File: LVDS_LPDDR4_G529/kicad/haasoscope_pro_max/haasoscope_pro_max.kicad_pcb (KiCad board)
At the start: 10 copper layers, 200 x 125 mm, 8 parts, among them IC1 ADC12DL500ACF_Aligned, U1 MT53D512M16D1DS_Aligned, U2 FT601Q_Aligned, U3 Ti90G529_Functions

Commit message: add labels for all lvds_rx nets
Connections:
- net Net-(IC1A-DA1+) renamed /fpga_adc/lvds_rx3_2_P
- net Net-(IC1A-DA1-) renamed /fpga_adc/lvds_rx3_2_N
- net Net-(IC1A-DA10+) renamed /fpga_adc/lvds_rx3_11_P
- net Net-(IC1A-DA10-) renamed /fpga_adc/lvds_rx3_11_N
- net Net-(IC1A-DA11+) renamed /fpga_adc/lvds_rx3_12_P
- net Net-(IC1A-DA11-) renamed /fpga_adc/lvds_rx3_12_N
- net Net-(IC1A-DA2+) renamed /fpga_adc/lvds_rx3_3_P
- net Net-(IC1A-DA2-) renamed /fpga_adc/lvds_rx3_3_N
- net Net-(IC1A-DA3+) renamed /fpga_adc/lvds_rx3_4_P
- net Net-(IC1A-DA3-) renamed /fpga_adc/lvds_rx3_4_N
- net Net-(IC1A-DA4+) renamed /fpga_adc/lvds_rx3_5_P
- net Net-(IC1A-DA4-) renamed /fpga_adc/lvds_rx3_5_N
- net Net-(IC1A-DA5+) renamed /fpga_adc/lvds_rx3_6_P
- net Net-(IC1A-DA5-) renamed /fpga_adc/lvds_rx3_6_N
- net Net-(IC1A-DA6+) renamed /fpga_adc/lvds_rx3_7_P
- net Net-(IC1A-DA6-) renamed /fpga_adc/lvds_rx3_7_N
- net Net-(IC1A-DA7+) renamed /fpga_adc/lvds_rx3_8_P
- net Net-(IC1A-DA7-) renamed /fpga_adc/lvds_rx3_8_N
- net Net-(IC1A-DA8+) renamed /fpga_adc/lvds_rx3_9_P
- net Net-(IC1A-DA8-) renamed /fpga_adc/lvds_rx3_9_N
- net Net-(IC1A-DA9+) renamed /fpga_adc/lvds_rx3_10_P
- net Net-(IC1A-DA9-) renamed /fpga_adc/lvds_rx3_10_N
- net Net-(IC1A-DASTR+) renamed /fpga_adc/lvds_rx3_13_P
- net Net-(IC1A-DASTR-) renamed /fpga_adc/lvds_rx3_13_N
- net Net-(IC1A-DC0+) renamed /fpga_adc/lvds_rx4_1_P
- net Net-(IC1A-DC0-) renamed /fpga_adc/lvds_rx4_1_N
- net Net-(IC1A-DC1+) renamed /fpga_adc/lvds_rx4_2_P
- net Net-(IC1A-DC1-) renamed /fpga_adc/lvds_rx4_2_N
- net Net-(IC1A-DC10+) renamed /fpga_adc/lvds_rx4_11_P
- net Net-(IC1A-DC10-) renamed /fpga_adc/lvds_rx4_11_N
- net Net-(IC1A-DC11+) renamed /fpga_adc/lvds_rx4_12_P
- net Net-(IC1A-DC11-) renamed /fpga_adc/lvds_rx4_12_N
- net Net-(IC1A-DC2+) renamed /fpga_adc/lvds_rx4_3_P
- net Net-(IC1A-DC2-) renamed /fpga_adc/lvds_rx4_3_N
- net Net-(IC1A-DC3+) renamed /fpga_adc/lvds_rx4_4_P
- net Net-(IC1A-DC3-) renamed /fpga_adc/lvds_rx4_4_N
- net Net-(IC1A-DC4+) renamed /fpga_adc/lvds_rx4_5_P
- net Net-(IC1A-DC4-) renamed /fpga_adc/lvds_rx4_5_N
- net Net-(IC1A-DC5+) renamed /fpga_adc/lvds_rx4_6_P
- net Net-(IC1A-DC5-) renamed /fpga_adc/lvds_rx4_6_N
- net Net-(IC1A-DC6+) renamed /fpga_adc/lvds_rx4_7_P
- net Net-(IC1A-DC6-) renamed /fpga_adc/lvds_rx4_7_N
- net Net-(IC1A-DC7+) renamed /fpga_adc/lvds_rx4_8_P
- net Net-(IC1A-DC7-) renamed /fpga_adc/lvds_rx4_8_N
- net Net-(IC1A-DC8+) renamed /fpga_adc/lvds_rx4_9_P
- net Net-(IC1A-DC8-) renamed /fpga_adc/lvds_rx4_9_N
- net Net-(IC1A-DC9+) renamed /fpga_adc/lvds_rx4_10_P
- net Net-(IC1A-DC9-) renamed /fpga_adc/lvds_rx4_10_N
- net Net-(IC1A-DCSTR+) renamed /fpga_adc/lvds_rx4_13_P
- net Net-(IC1A-DCSTR-) renamed /fpga_adc/lvds_rx4_13_N
- net Net-(IC1B-DB1+) renamed /fpga_adc/lvds_rx1_2_P
- net Net-(IC1B-DB1-) renamed /fpga_adc/lvds_rx1_2_N
- net Net-(IC1B-DB10+) renamed /fpga_adc/lvds_rx1_11_P
- net Net-(IC1B-DB10-) renamed /fpga_adc/lvds_rx1_11_N
- net Net-(IC1B-DB11+) renamed /fpga_adc/lvds_rx1_12_P
- net Net-(IC1B-DB11-) renamed /fpga_adc/lvds_rx1_12_N
- net Net-(IC1B-DB2+) renamed /fpga_adc/lvds_rx1_3_P
- net Net-(IC1B-DB2-) renamed /fpga_adc/lvds_rx1_3_N
- net Net-(IC1B-DB3+) renamed /fpga_adc/lvds_rx1_4_P
- net Net-(IC1B-DB3-) renamed /fpga_adc/lvds_rx1_4_N
- net Net-(IC1B-DB4+) renamed /fpga_adc/lvds_rx1_5_P
- net Net-(IC1B-DB4-) renamed /fpga_adc/lvds_rx1_5_N
- net Net-(IC1B-DB5+) renamed /fpga_adc/lvds_rx1_6_P
- net Net-(IC1B-DB5-) renamed /fpga_adc/lvds_rx1_6_N
- net Net-(IC1B-DB6+) renamed /fpga_adc/lvds_rx1_7_P
- net Net-(IC1B-DB6-) renamed /fpga_adc/lvds_rx1_7_N
- net Net-(IC1B-DB7+) renamed /fpga_adc/lvds_rx1_8_P
- net Net-(IC1B-DB7-) renamed /fpga_adc/lvds_rx1_8_N
- net Net-(IC1B-DB8+) renamed /fpga_adc/lvds_rx1_9_P
- net Net-(IC1B-DB8-) renamed /fpga_adc/lvds_rx1_9_N
- net Net-(IC1B-DB9+) renamed /fpga_adc/lvds_rx1_10_P
- net Net-(IC1B-DB9-) renamed /fpga_adc/lvds_rx1_10_N
- net Net-(IC1B-DBSTR+) renamed /fpga_adc/lvds_rx1_13_P
- net Net-(IC1B-DBSTR-) renamed /fpga_adc/lvds_rx1_13_N
- net Net-(IC1B-DD0+) renamed /fpga_adc/lvds_rx2_1_P
- net Net-(IC1B-DD0-) renamed /fpga_adc/lvds_rx2_1_N
- net Net-(IC1B-DD1+) renamed /fpga_adc/lvds_rx2_2_P
- net Net-(IC1B-DD1-) renamed /fpga_adc/lvds_rx2_2_N
- net Net-(IC1B-DD10+) renamed /fpga_adc/lvds_rx2_11_P
- net Net-(IC1B-DD10-) renamed /fpga_adc/lvds_rx2_11_N
- net Net-(IC1B-DD11+) renamed /fpga_adc/lvds_rx2_12_P
- net Net-(IC1B-DD11-) renamed /fpga_adc/lvds_rx2_12_N
- net Net-(IC1B-DD2+) renamed /fpga_adc/lvds_rx2_3_P
- net Net-(IC1B-DD2-) renamed /fpga_adc/lvds_rx2_3_N
- net Net-(IC1B-DD3+) renamed /fpga_adc/lvds_rx2_4_P
- net Net-(IC1B-DD3-) renamed /fpga_adc/lvds_rx2_4_N
- net Net-(IC1B-DD4+) renamed /fpga_adc/lvds_rx2_5_P
- net Net-(IC1B-DD4-) renamed /fpga_adc/lvds_rx2_5_N
- net Net-(IC1B-DD5+) renamed /fpga_adc/lvds_rx2_6_P
- net Net-(IC1B-DD5-) renamed /fpga_adc/lvds_rx2_6_N
- net Net-(IC1B-DD6+) renamed /fpga_adc/lvds_rx2_7_P
- net Net-(IC1B-DD6-) renamed /fpga_adc/lvds_rx2_7_N
- net Net-(IC1B-DD7+) renamed /fpga_adc/lvds_rx2_8_P
- net Net-(IC1B-DD7-) renamed /fpga_adc/lvds_rx2_8_N
- net Net-(IC1B-DD8+) renamed /fpga_adc/lvds_rx2_9_P
- net Net-(IC1B-DD8-) renamed /fpga_adc/lvds_rx2_9_N
- net Net-(IC1B-DD9+) renamed /fpga_adc/lvds_rx2_10_P
- net Net-(IC1B-DD9-) renamed /fpga_adc/lvds_rx2_10_N
- net Net-(IC1B-DDSTR+) renamed /fpga_adc/lvds_rx2_13_P
- net Net-(IC1B-DDSTR-) renamed /fpga_adc/lvds_rx2_13_N
- net Net-(IC1C-DACLK+) renamed /fpga_adc/lvds_rx_top_clkin3_P
- net Net-(IC1C-DACLK-) renamed /fpga_adc/lvds_rx_top_clkin3_N
- net Net-(IC1C-DBCLK+) renamed /fpga_adc/lvds_rx_top_clkin1_P
- net Net-(IC1C-DBCLK-) renamed /fpga_adc/lvds_rx_top_clkin1_N
- net Net-(IC1C-DCCLK+) renamed /fpga_adc/lvds_rx_top_clkin4_P
- net Net-(IC1C-DCCLK-) renamed /fpga_adc/lvds_rx_top_clkin4_N
- net Net-(IC1C-DDCLK+) renamed /fpga_adc/lvds_rx_top_clkin2_P
- net Net-(IC1C-DDCLK-) renamed /fpga_adc/lvds_rx_top_clkin2_N

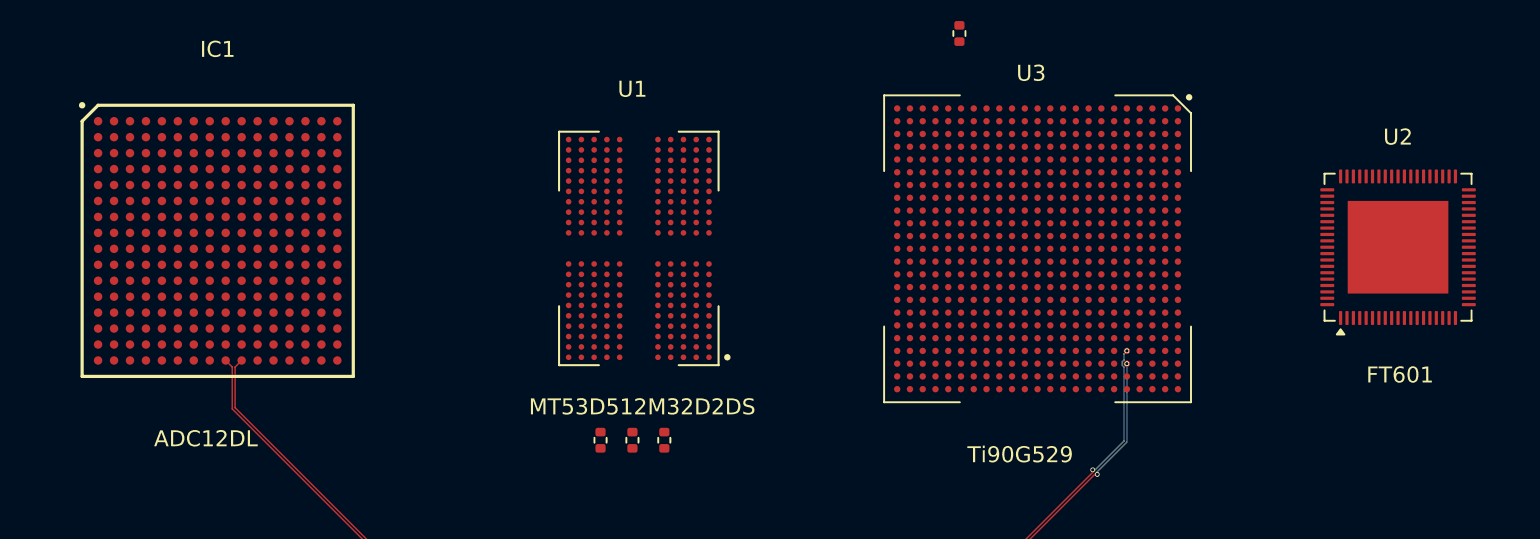
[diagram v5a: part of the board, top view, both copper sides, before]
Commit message: vias in pad
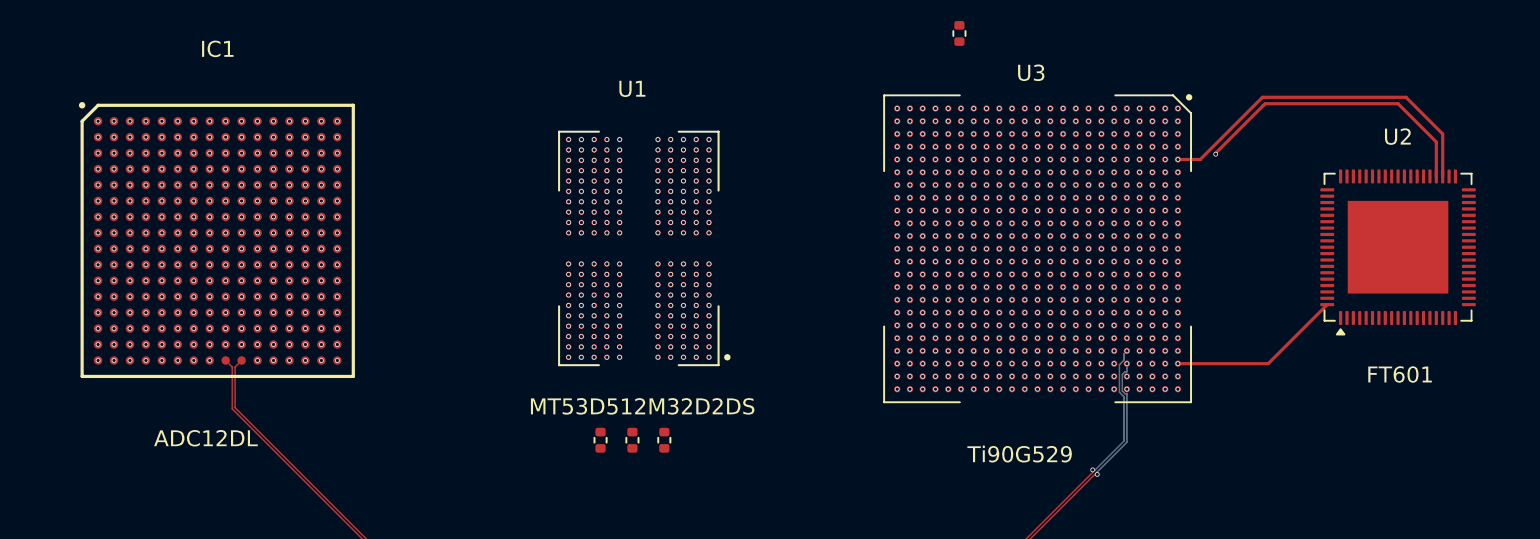
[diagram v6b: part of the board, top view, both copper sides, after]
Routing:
- net Net-(U2A-DATA_2): track 0.00 -> 24.4 mm, vias 0 -> 2
- net Net-(U2A-DATA_1): track 0.00 -> 21.8 mm, vias 0 -> 1
- net Net-(U2A-DATA_31): track 0.00 -> 10.9 mm, vias 0 -> 1
- net unconnected-(U3J-NC-PadW15): vias 0 -> 1
- net unconnected-(U3J-NC-PadW14): vias 0 -> 1
- net unconnected-(U3J-NC-PadW13): vias 0 -> 1
- net unconnected-(U3J-NC-PadW11): vias 0 -> 1
- net unconnected-(U3J-NC-PadW10): vias 0 -> 1
- net unconnected-(U3J-NC-PadV16): vias 0 -> 1
- net unconnected-(U3J-GPIOT_P_33-PadF17): vias 0 -> 1
- net unconnected-(U3J-GPIOT_P_23_PLLIN0-PadD23): vias 0 -> 1
- net unconnected-(U3J-GPIOT_N_34-PadG18): vias 0 -> 1
- net unconnected-(U3J-GPIOT_N_33-PadG17): vias 0 -> 1
- net unconnected-(U3J-GPIOT_N_23-PadC23): vias 0 -> 1
- net unconnected-(U3J-GPIOL_44-PadW20): vias 0 -> 1
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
